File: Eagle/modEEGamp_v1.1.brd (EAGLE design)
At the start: 111.4 x 64.8 mm, 131 parts, among them IC2 INA217P, IC204 TLC277P, IC3 TLC277P, IC4 INA217P, IC5 TLC277P, P1 20k, P203 20k, Q1 BC547, Q2 BC557, Q202 BC557, Q204 BC557, Q206 BC547, Q208 BC547, Q3 BC547, Q4 BC557

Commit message: Finished up chanes to DB25
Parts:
- removed C13, C14, C29, C30: 100nF, resistor:C1206
- removed IC3, IC5: TLC277P, BURR:DIL-08
- removed R1, R2: 10k, resistor:0207/2V
- removed SJ1, SJ10, SJ11, SJ12, SJ2, SJ3, SJ4, SJ5, SJ6, SJ7, SJ8, SJ9: (no value), jumper:SJ
- added IC1: (no value), v-reg-micrel:SOT23-5
- moved R6 38.1 mm to (41.9, 41.9)
- moved C219 13.1 mm to (36.8, 34.3)
- moved R218 2.84 mm to (41.9, 44.5)
- moved C19 2.54 mm to (74.9, 53.3)
- moved Q204 2.54 mm to (19.1, 53.3)
- moved Q208 2.54 mm to (14.0, 53.3)
- moved U$3 2.54 mm to (68.6, 53.3)
- moved C15 2.54 mm to (70.5, 22.2)
- moved CH2- 2.54 mm to (2.54, 26.7)
- moved P1 2.54 mm to (48.3, 26.7)
- moved R14 2.54 mm to (40.6, 26.7)
- moved R15 2.54 mm to (36.8, 27.9)
- moved R5 2.54 mm to (27.9, 27.9)
- moved R8 2.54 mm to (6.35, 26.7)
- moved TPIAB 2.54 mm to (32.4, 27.9)
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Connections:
- removed net N$68: C30.1, IC5.8
- removed net N$69: SJ1.2, X2.25
- removed net N$70: SJ2.2, X2.13
- removed net N$71: SJ3.2, X2.24
- removed net N$72: SJ4.2, X2.12
- removed net N$73: SJ5.2, X2.23
- removed net N$74: SJ6.2, X2.11
- removed net N$75: SJ7.2, X2.22
- removed net N$76: SJ8.2, X2.10
- removed net N$77: SJ12.2, X2.8
- removed net N$78: SJ11.2, X2.20
- removed net N$79: SJ9.2, X2.21
- removed net N$80: SJ10.2, X2.9
- removed net N$81: SJ1.1, SJ10.1, SJ11.1, SJ12.1, SJ2.1, SJ3.1, SJ4.1, SJ5.1, SJ6.1, SJ7.1, SJ8.1, SJ9.1
- removed net N$9: IC5.3, R1.2, R2.2
- net +5V/2: now also IC1.1, IC1.3; no longer C14.2, C30.2, IC3.8, R2.1
- net AGND: now also IC1.2; no longer C13.1, C29.1, IC3.4, R1.1
- net N$12: now also IC204.5; no longer IC204.3
- net N$13: now also IC204.3; no longer IC3.3
- net N$2: now also IC1.5; no longer IC5.1, IC5.2
- net N$3: now also U$1.12, X2.10, X2.11, X2.12, X2.13, X2.20, X2.21, X2.22, X2.23, X2.24, X2.25, X2.8, X2.9; no longer C29.2, IC5.4
- net N$35: now also IC204.1, IC204.2; no longer IC3.1, IC3.2
- net N$52: now also IC204.6, IC204.7; no longer IC204.1, IC204.2
- net VCOM: no longer C13.2, C14.1
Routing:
- net N$66: track 162.8 -> 62.7 mm
- net AGND: track 403.4 -> 347.4 mm, vias 18 -> 16
- net N$3: track 3.54 -> 56.7 mm
- net N$81: track 37.7 -> 0.00 mm
- net N$9: track 13.2 -> 0.00 mm
- net N$73: track 8.44 -> 0.00 mm
- net N$79: track 8.25 -> 0.00 mm
- net N$71: track 8.24 -> 0.00 mm
- net N$78: track 8.17 -> 0.00 mm
- net N$75: track 8.16 -> 0.00 mm
- net N$69: track 8.15 -> 0.00 mm
- net +5V/2: track 290.3 -> 298.3 mm, vias 15 -> 16
- net VCOM: track 374.5 -> 380.2 mm
- net N$13: track 30.6 -> 26.7 mm
- net N$52: track 12.5 -> 8.67 mm
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- added copper zone on layer 16, net AGND
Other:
- board size 111.4 x 64.8 mm -> 111.1 x 72.4 mm

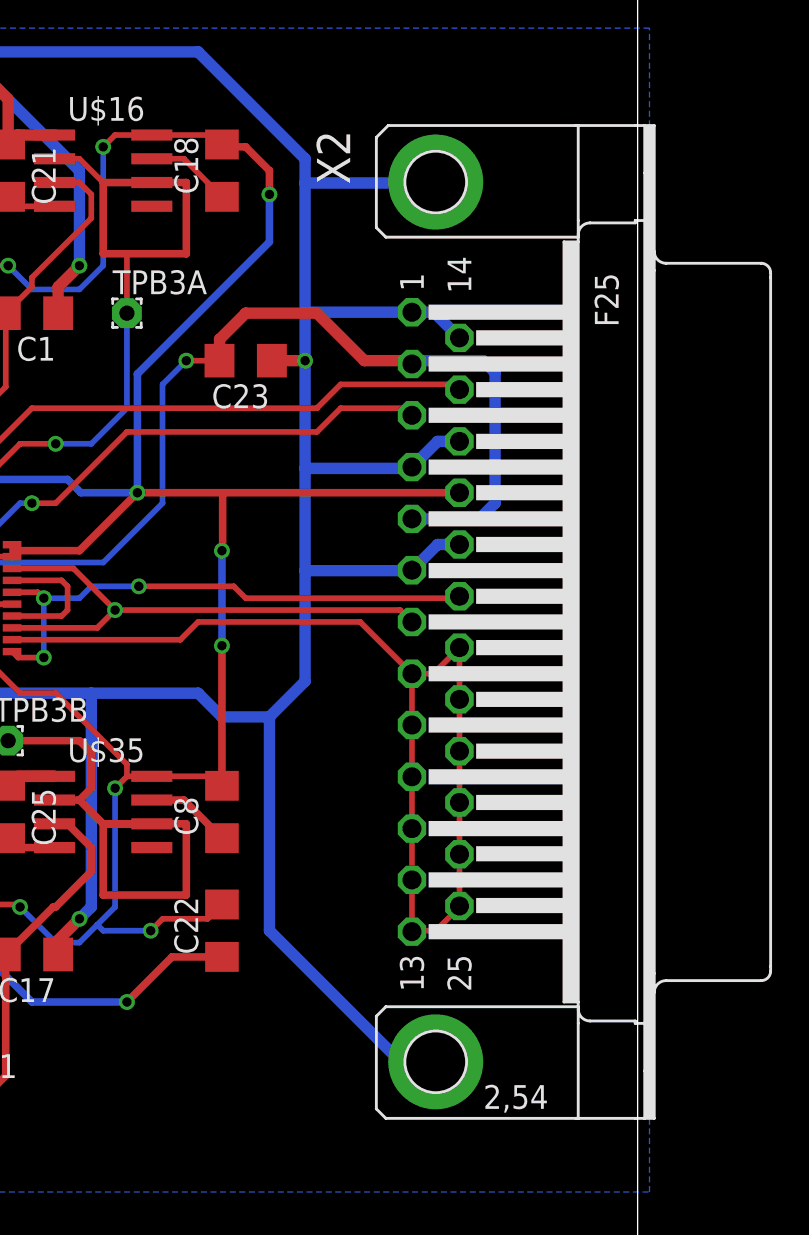
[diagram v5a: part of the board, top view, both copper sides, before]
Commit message: Corrected connector positions
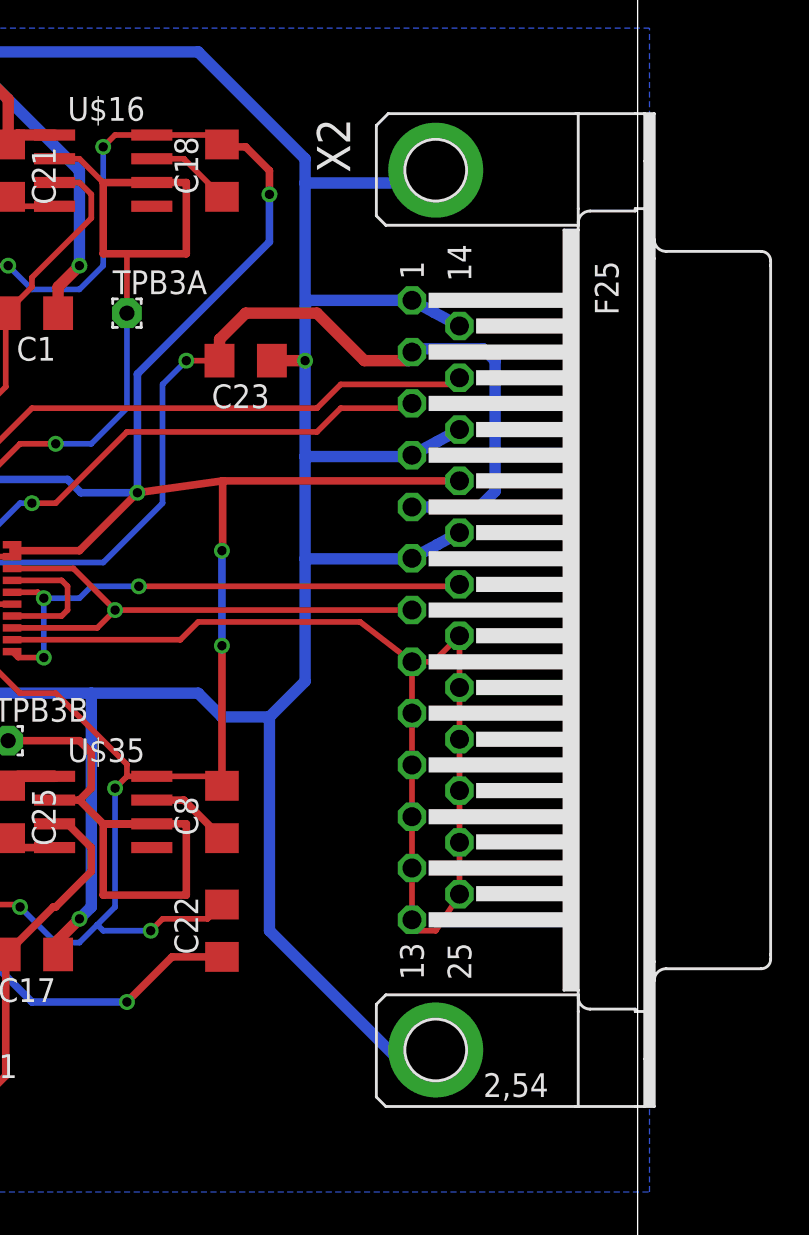
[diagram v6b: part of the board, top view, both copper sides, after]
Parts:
- moved X2 0.63 mm to (100.3, 36.2)
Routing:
- net +5V/2: track 298.3 -> 299.0 mm
- net N$3: track 56.7 -> 57.4 mm

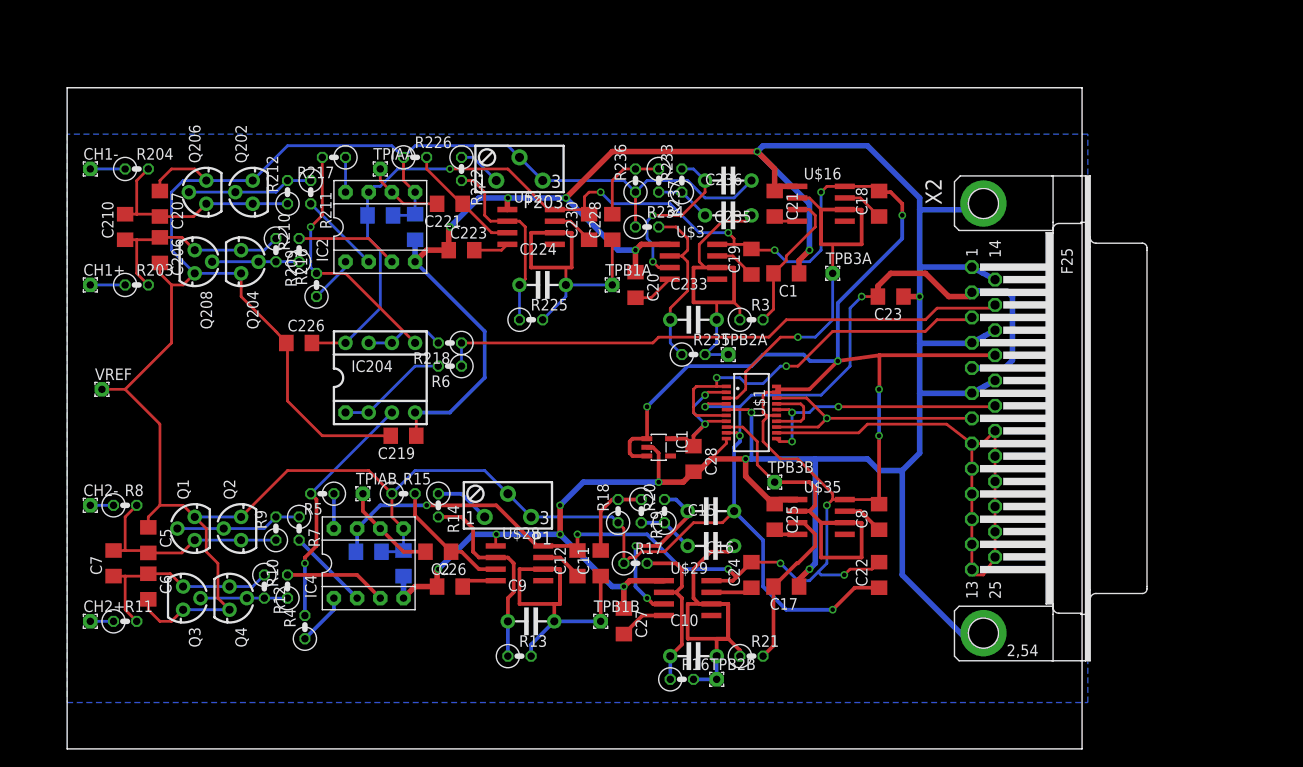
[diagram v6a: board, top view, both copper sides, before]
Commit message: Added DIN 42802 jacks & power for active electrodes
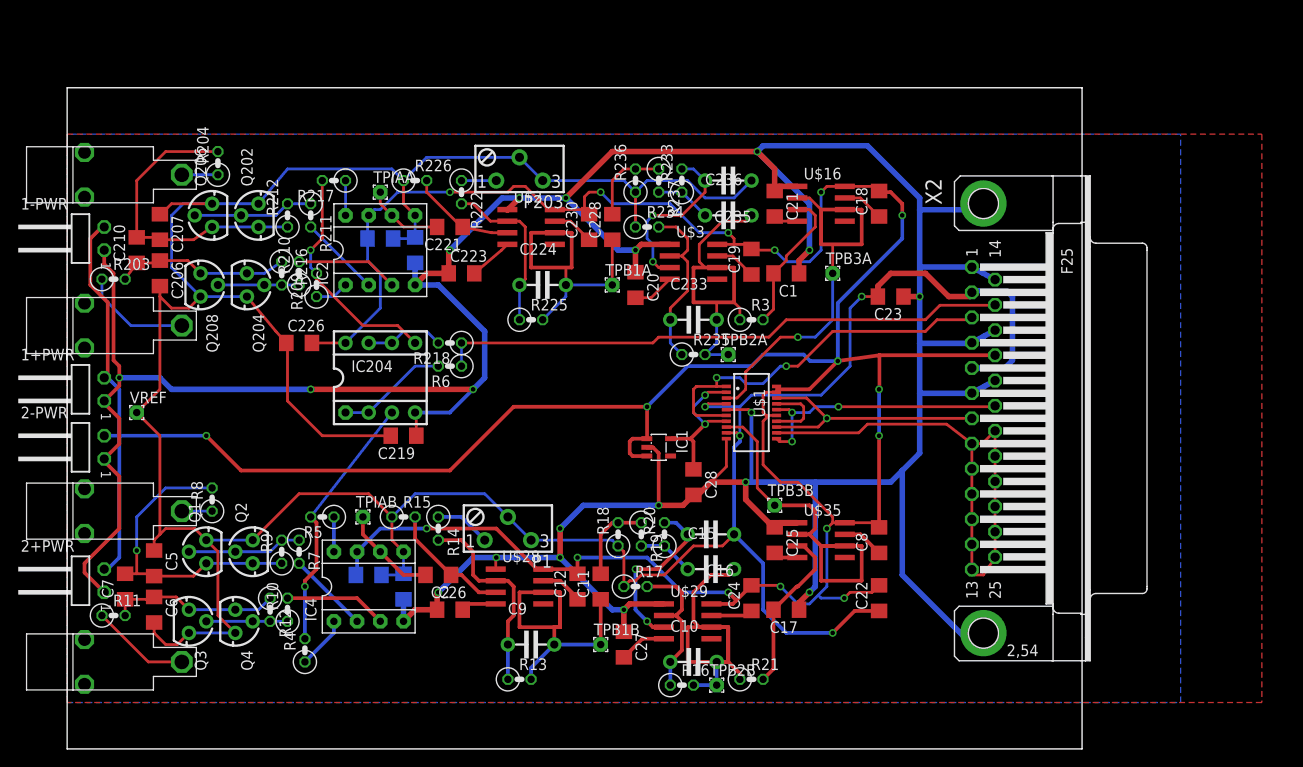
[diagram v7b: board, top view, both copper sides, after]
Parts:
- removed CH1+, CH1-, CH2+, CH2-: (no value), WIREPAD:1,6/0,8
- added 1+PWR, 1-PWR, 2+PWR, 2-PWR: TSW-102-02-S-S-RA, con-samtec:TSW-102-02-S-S-RA
- added C1+, C1-, C2+, C2-: DIN42802, modEEG:DIN42802
- moved R8 9.55 mm to (15.9, 27.3), turned to 90 degrees
- moved R204 8.91 mm to (16.5, 64.1), turned to 90 degrees
- moved VREF 4.58 mm to (7.62, 36.8)
- moved C210 2.84 mm to (7.62, 54.6)
- moved C7 2.84 mm to (6.35, 17.8)
- moved Q1 2.84 mm to (15.2, 21.6)
- moved Q2 2.84 mm to (20.3, 21.6)
- moved Q204 2.62 mm to (19.7, 50.8)
- moved Q208 2.62 mm to (14.6, 50.8)
- moved R203 2.62 mm to (5.08, 51.4)
- moved C6 2.62 mm to (9.53, 15.2)
- moved Q3 2.62 mm to (13.3, 14.0)
- moved R12 2.62 mm to (22.2, 15.2)
- moved Q4 2.62 mm to (18.4, 14.0)
- moved R209 2.62 mm to (23.5, 52.1)
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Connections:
- net +5V/2: now also 1+PWR.2, 1-PWR.2, 2+PWR.2, 2-PWR.2
- net AGND: now also 1+PWR.1, 1-PWR.1, 2+PWR.1, 2-PWR.1
- net N$11: now also C1+.P$1; no longer CH1+.1
- net N$24: now also C2-.P$1; no longer CH2-.1
- net N$26: now also C2+.P$1; no longer CH2+.1
- net N$6: now also C1-.P$1; no longer CH1-.1
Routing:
- net +5V/2: track 299.0 -> 405.9 mm, vias 16 -> 17
- net AGND: track 347.4 -> 438.3 mm, vias 16 -> 19
- net N$19: track 23.9 -> 33.6 mm, vias 0 -> 1
- net N$32: track 23.9 -> 33.5 mm
- net N$26: track 2.54 -> 10.9 mm
- net N$11: track 3.81 -> 12.0 mm
- net N$23: track 23.2 -> 18.8 mm
- net N$43: track 23.2 -> 19.1 mm
- net VCOM: track 380.5 -> 377.1 mm
- net ADIN1: track 22.5 -> 25.1 mm
- net N$38: track 21.0 -> 18.5 mm
- net N$12: track 27.4 -> 25.3 mm
- net N$13: track 26.7 -> 28.6 mm
- net N$47: track 27.2 -> 25.3 mm
- net N$44: track 18.5 -> 16.6 mm
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- added copper zone on layer 1, net VCOM
- added copper zone on layer 16, net VCOM
- removed copper zone on layer 16, net AGND

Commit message: Added indicator LEDs
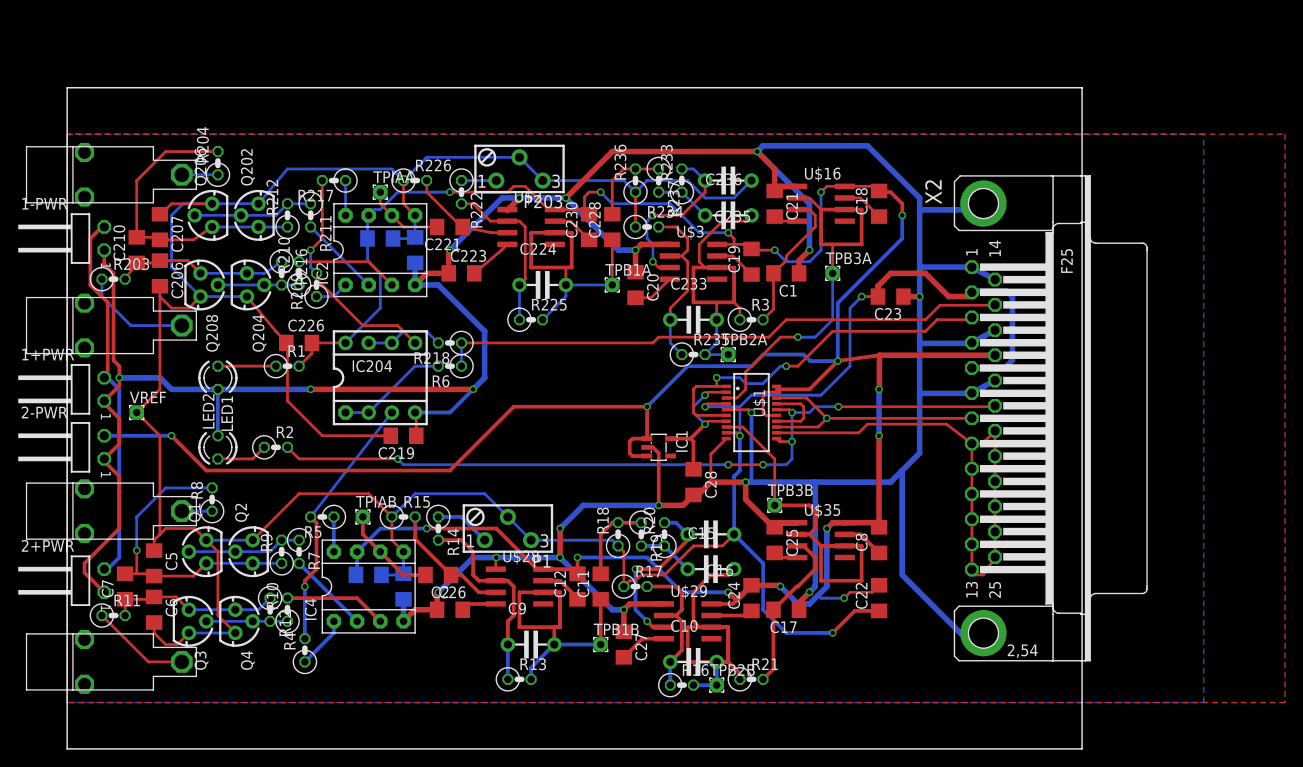
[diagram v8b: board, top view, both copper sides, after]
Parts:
- added LED1, LED2: (no value), led:LED3MM
- added R1, R2: (no value), resistor:0207/2V
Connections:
- new net N$67: LED2.A, R2.1
- new net N$9: LED1.A, R1.1
- net +5V/2: now also R1.2
- net AGND: now also LED1.K, LED2.K
- net N$8: now also R2.2
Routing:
- net N$8: track 29.4 -> 87.6 mm, vias 3 -> 6
- net +5V/2: track 405.9 -> 392.8 mm
- net N$9: track 0.00 -> 6.35 mm
- net N$67: track 0.00 -> 5.61 mm
- net AGND: track 438.3 -> 443.4 mm
